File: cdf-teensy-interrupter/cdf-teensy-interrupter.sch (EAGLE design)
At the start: 20 parts

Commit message: wip
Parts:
- added EMERGENCY: SWITCH-MOMENTARY-2PTH, SparkFun-Electromechanical:SWITCH-MOMENTARY-2PTH
- added R7: 220, rcl:R-US_0204/7
- added SP1: SPEAKER/PS12, adafruit:SPEAKER/PS12
- added T1: BC337, transistor:BC337
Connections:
- new net EMERGENCY: EMERGENCY.1, U$2.11/MOSI
- new net N$11: SP1.+, T1.C, U$6.C
- new net N$7: R7.1, T1.B
- net +3V3: now also R3.2
- net +5V: now also R5.2, SP1.-; no longer R3.2
- net GND: now also EMERGENCY.2, T1.E; no longer U$6.C
- net TX: now also R7.2; no longer R5.2
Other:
- note added: "TL1105LF250Q"
- moved on the sheet: R5, U$6
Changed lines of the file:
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@@
 <part name="R2" library="rcl" deviceset="R-US_" device="0204/7" value="100K"/>
 <part name="R3" library="rcl" deviceset="R-US_" device="0204/7" value="3.3K"/>
-<part name="P+1" library="supply1" deviceset="+5V" device=""/>
 <part name="GND3" library="supply1" deviceset="GND" device=""/>
 <part name="GND8" library="supply1" deviceset="GND" device=""/>
@@
 <part name="GND10" library="supply1" deviceset="GND" device=""/>
 <part name="R5" library="rcl" deviceset="R-US_" device="0204/7" value="68"/>
-<part name="GND11" library="supply1" deviceset="GND" device=""/>
 <part name="R6" library="rcl" deviceset="R-US_" device="0204/7" value="330"/>
 <part name="LED1" library="adafruit" deviceset="LED" device="5MM"/>
@@
 <part name="PULSE_WIDTH" library="Bourns" deviceset="POTENTIOMETER" device="PTV09A_VERTICAL" value="10K PTV09A-4025F-B103"/>
 <part name="P+6" library="supply1" deviceset="+5V" device=""/>
+<part name="+3V6" library="supply1" deviceset="+3V3" device=""/>
+<part name="GND14" library="supply1" deviceset="GND" device=""/>
+<part name="EMERGENCY" library="SparkFun-Electromechanical" deviceset="SWITCH-MOMENTARY-2" device="PTH"/>
+<part name="SP1" library="adafruit" deviceset="SPEAKER" device="/PS12"/>
+<part name="T1" library="transistor" deviceset="BC337" device=""/>
+<part name="R7" library="rcl" deviceset="R-US_" device="0204/7" value="220"/>
+<part name="GND16" library="supply1" deviceset="GND" device=""/>
+<part name="P+1" library="supply1" deviceset="+5V" device=""/>
 </parts>
 <sheets>
 <sheet>
 <plain>
+<text x="17.78" y="63.5" size="1.778" layer="96" rot="R270">
+TL1105LF250Q
+</text>
 </plain>
 <instances>
@@
 <instance part="U$1" gate="G$1" x="-30.48" y="83.82"/>
 <instance part="MIDI_MODE" gate="G$1" x="127" y="66.04" smashed="yes" rot="R270"/>
-<instance part="U$6" gate="G$1" x="137.16" y="22.86" rot="R90"/>
+<instance part="U$6" gate="G$1" x="10.16" y="35.56"/>
 <instance part="R1" gate="G$1" x="-7.62" y="81.28"/>
 <instance part="D1" gate="G$1" x="0" y="78.74" rot="R90"/>
@@
 <instance part="R2" gate="G$1" x="22.86" y="91.44" rot="R90"/>
 <instance part="R3" gate="G$1" x="33.02" y="91.44" rot="R90"/>
-<instance part="P+1" gate="1" x="33.02" y="101.6"/>
 <instance part="GND3" gate="1" x="22.86" y="68.58"/>
 <instance part="GND8" gate="1" x="149.86" y="96.52" rot="R90"/>
 <instance part="GND9" gate="1" x="149.86" y="111.76" rot="R90"/>
 <instance part="GND10" gate="1" x="134.62" y="63.5" rot="R90"/>
-<instance part="R5" gate="G$1" x="127" y="22.86" rot="R180"/>
-<instance part="GND11" gate="1" x="147.32" y="22.86" rot="R90"/>
+<instance part="R5" gate="G$1" x="10.16" y="50.8" rot="R90"/>
 <instance part="R6" gate="G$1" x="-17.78" y="48.26" rot="R270"/>
 <instance part="LED1" gate="G$1" x="-17.78" y="38.1"/>
@@
 </instance>
 <instance part="P+6" gate="1" x="-17.78" y="58.42"/>
+<instance part="+3V6" gate="G$1" x="33.02" y="101.6"/>
+<instance part="GND14" gate="1" x="137.16" y="38.1" rot="R90"/>
+<instance part="EMERGENCY" gate="G$1" x="124.46" y="38.1" smashed="yes">
+<attribute name="NAME" x="121.92" y="40.64" size="1.778" layer="95"/>
+</instance>
+<instance part="SP1" gate="S1" x="0" y="33.02" rot="R90"/>
+<instance part="T1" gate="G$1" x="12.7" y="17.78" rot="MR0"/>
+<instance part="R7" gate="G$1" x="27.94" y="17.78"/>
+<instance part="GND16" gate="1" x="10.16" y="7.62"/>
+<instance part="P+1" gate="1" x="10.16" y="63.5"/>
 </instances>
 <busses>
@@
 </segment>
 <segment>
-<pinref part="U$6" gate="G$1" pin="C"/>
-<pinref part="GND11" gate="1" pin="GND"/>
-<wire x1="144.78" y1="22.86" x2="142.24" y2="22.86" width="0.1524" layer="91"/>
-</segment>
-<segment>
 <pinref part="LED1" gate="G$1" pin="C"/>
 <pinref part="GND12" gate="1" pin="GND"/>
@@
 <pinref part="GND13" gate="1" pin="GND"/>
 </segment>
+<segment>
+<pinref part="GND14" gate="1" pin="GND"/>
+<wire x1="134.62" y1="38.1" x2="129.54" y2="38.1" width="0.1524" layer="91"/>
+<pinref part="EMERGENCY" gate="G$1" pin="2"/>
+</segment>
+<segment>
+<pinref part="T1" gate="G$1" pin="E"/>
+<pinref part="GND16" gate="1" pin="GND"/>
+<wire x1="10.16" y1="10.16" x2="10.16" y2="12.7" width="0.1524" layer="91"/>
+</segment>
 </net>
 <net name="+5V" class="0">
-<segment>
-<pinref part="R3" gate="G$1" pin="2"/>
-<pinref part="P+1" gate="1" pin="+5V"/>
-<wire x1="33.02" y1="99.06" x2="33.02" y2="96.52" width="0.1524" layer="91"/>
-</segment>
 <segment>
 <pinref part="U$2" gate="G$1" pin="VIN"/>
@@
 <wire x1="-17.78" y1="53.34" x2="-17.78" y2="55.88" width="0.1524" layer="91"/>
 <pinref part="P+6" gate="1" pin="+5V"/>
+</segment>
+<segment>
+<pinref part="SP1" gate="S1" pin="-"/>
+<wire x1="0" y1="38.1" x2="0" y2="58.42" width="0.1524" layer="91"/>
+<wire x1="0" y1="58.42" x2="10.16" y2="58.42" width="0.1524" layer="91"/>
+<pinref part="R5" gate="G$1" pin="2"/>
+<wire x1="10.16" y1="58.42" x2="10.16" y2="55.88" width="0.1524" layer="91"/>
+<pinref part="P+1" gate="1" pin="+5V"/>
+<wire x1="10.16" y1="58.42" x2="10.16" y2="60.96" width="0.1524" layer="91"/>
+<junction x="10.16" y="58.42"/>
 </segment>
 </net>
@@
 <net name="TX" class="0">
 <segment>
-<pinref part="R5" gate="G$1" pin="2"/>
-<wire x1="121.92" y1="22.86" x2="116.84" y2="22.86" width="0.1524" layer="91"/>
-<label x="116.84" y="22.86" size="1.778" layer="95"/>
-</segment>
-<segment>
 <pinref part="U$2" gate="G$1" pin="21/A7/PWM"/>
 <wire x1="43.18" y1="17.78" x2="33.02" y2="17.78" width="0.1524" layer="91"/>
 <label x="33.02" y="17.78" size="1.778" layer="95"/>
+<pinref part="R7" gate="G$1" pin="2"/>
 </segment>
 </net>
@@
 <pinref part="R5" gate="G$1" pin="1"/>
 <pinref part="U$6" gate="G$1" pin="A"/>
-<wire x1="134.62" y1="22.86" x2="132.08" y2="22.86" width="0.1524" layer="91"/>
+<wire x1="10.16" y1="38.1" x2="10.16" y2="45.72" width="0.1524" layer="91"/>
 </segment>
 </net>
@@
 <pinref part="+3V5" gate="G$1" pin="+3V3"/>
 </segment>
+<segment>
+<pinref part="R3" gate="G$1" pin="2"/>
+<wire x1="33.02" y1="99.06" x2="33.02" y2="96.52" width="0.1524" layer="91"/>
+<pinref part="+3V6" gate="G$1" pin="+3V3"/>
+</segment>
 </net>
 <net name="LCD_EN" class="0">
@@
 <pinref part="R4" gate="G$1" pin="2"/>
 <wire x1="55.88" y1="93.98" x2="66.04" y2="93.98" width="0.1524" layer="91"/>
+</segment>
+</net>
+<net name="EMERGENCY" class="0">
+<segment>
+<pinref part="EMERGENCY" gate="G$1" pin="1"/>
+<wire x1="119.38" y1="38.1" x2="106.68" y2="38.1" width="0.1524" layer="91"/>
+<label x="99.06" y="38.1" size="1.778" layer="95"/>
+</segment>
+<segment>
+<pinref part="U$2" gate="G$1" pin="11/MOSI"/>
+<wire x1="43.18" y1="43.18" x2="33.02" y2="43.18" width="0.1524" layer="91"/>
+<label x="25.4" y="43.18" size="1.778" layer="95"/>
+</segment>
+</net>
+<net name="N$7" class="0">
+<segment>
+<pinref part="R7" gate="G$1" pin="1"/>
+<pinref part="T1" gate="G$1" pin="B"/>
+<wire x1="15.24" y1="17.78" x2="22.86" y2="17.78" width="0.1524" layer="91"/>
+</segment>
+</net>
+<net name="N$11" class="0">
+<segment>
+<pinref part="SP1" gate="S1" pin="+"/>
+<wire x1="0" y1="25.4" x2="0" y2="27.94" width="0.1524" layer="91"/>
+<pinref part="U$6" gate="G$1" pin="C"/>
+<wire x1="10.16" y1="22.86" x2="10.16" y2="25.4" width="0.1524" layer="91"/>
+<pinref part="T1" gate="G$1" pin="C"/>
+<wire x1="10.16" y1="25.4" x2="10.16" y2="30.48" width="0.1524" layer="91"/>
+<wire x1="0" y1="25.4" x2="10.16" y2="25.4" width="0.1524" layer="91"/>
+<junction x="10.16" y="25.4"/>
 </segment>
 </net>
@@
 </schematic>
 </drawing>
+<compatibility>
+<note version="6.3" minversion="6.2.2" severity="warning">
+Since Version 6.2.2 text objects can contain more than one line,
+which will not be processed correctly with this version.
+</note>
+</compatibility>
 </eagle>

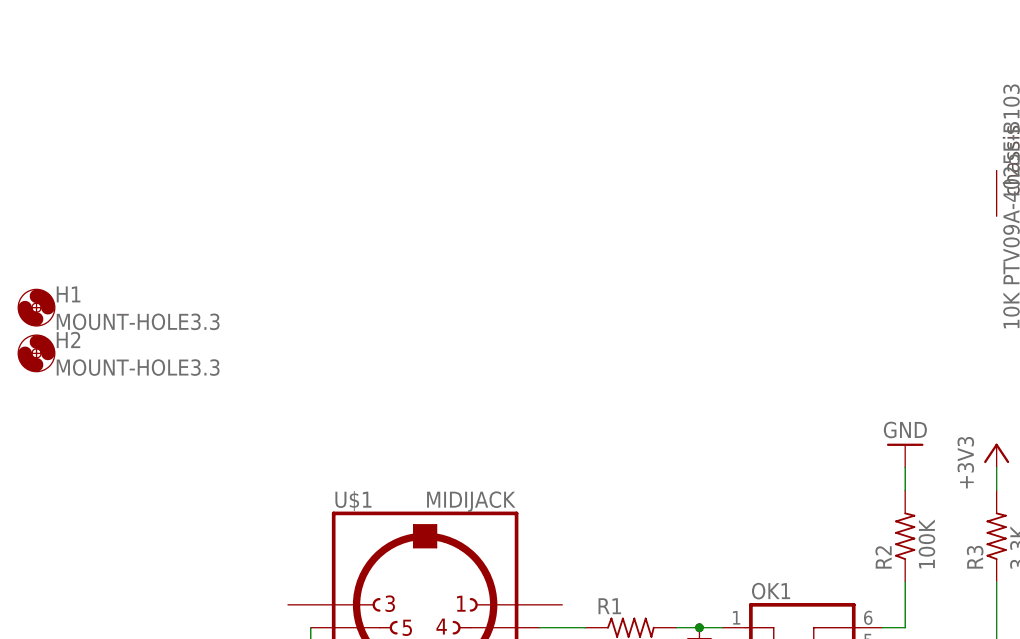
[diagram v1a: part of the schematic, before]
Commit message: add usb connector
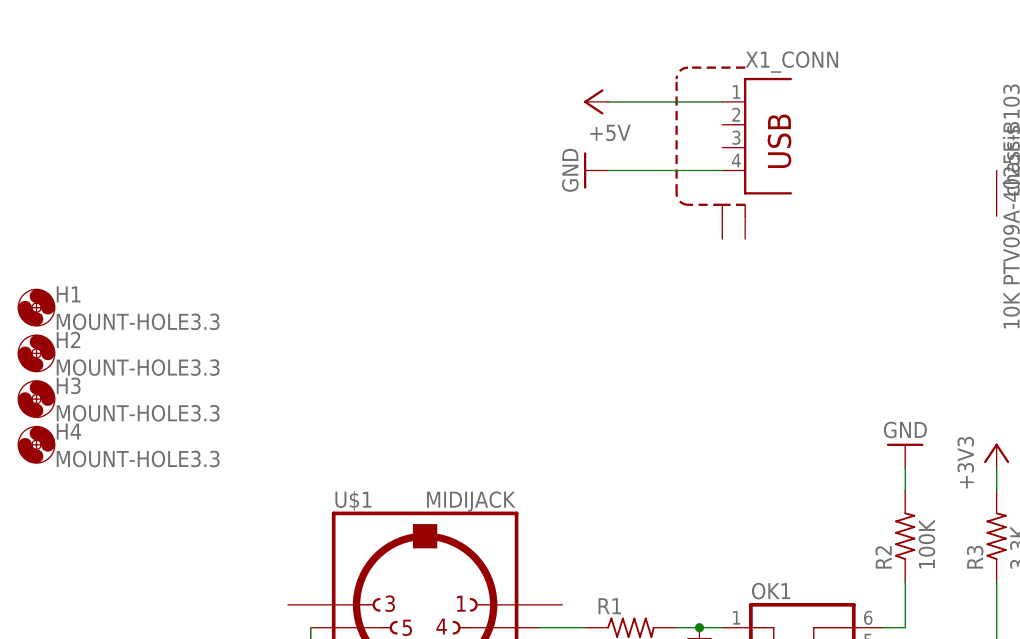
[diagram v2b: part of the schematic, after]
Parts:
- added H3, H4: MOUNT-HOLE3.3, holes:MOUNT-HOLE3.3
- added X1: (no value), keves:TE-292304-1
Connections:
- net +5V: now also X1_CONN.1
- net GND: now also X1_CONN.4
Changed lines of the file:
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@@
 <?xml version="1.0" encoding="utf-8"?>
 <!DOCTYPE eagle SYSTEM "eagle.dtd">
-<eagle version="7.5.0">
+<eagle version="7.3.0">
 <drawing>
 <settings>
@@
 <layers>
 <layer number="1" name="Top" color="4" fill="1" visible="no" active="no"/>
+<layer number="2" name="Route2" color="1" fill="3" visible="no" active="no"/>
+<layer number="3" name="Route3" color="4" fill="3" visible="no" active="no"/>
+<layer number="4" name="Route4" color="1" fill="4" visible="no" active="no"/>
+<layer number="5" name="Route5" color="4" fill="4" visible="no" active="no"/>
+<layer number="6" name="Route6" color="1" fill="8" visible="no" active="no"/>
+<layer number="7" name="Route7" color="4" fill="8" visible="no" active="no"/>
+<layer number="8" name="Route8" color="1" fill="2" visible="no" active="no"/>
+<layer number="9" name="Route9" color="4" fill="2" visible="no" active="no"/>
+<layer number="10" name="Route10" color="1" fill="7" visible="no" active="no"/>
+<layer number="11" name="Route11" color="4" fill="7" visible="no" active="no"/>
+<layer number="12" name="Route12" color="1" fill="5" visible="no" active="no"/>
+<layer number="13" name="Route13" color="4" fill="5" visible="no" active="no"/>
+<layer number="14" name="Route14" color="1" fill="6" visible="no" active="no"/>
+<layer number="15" name="Route15" color="4" fill="6" visible="no" active="no"/>
 <layer number="16" name="Bottom" color="1" fill="1" visible="no" active="no"/>
 <layer number="17" name="Pads" color="2" fill="1" visible="no" active="no"/>
@@
 <layer number="56" name="wert" color="7" fill="1" visible="no" active="no"/>
 <layer number="57" name="tCAD" color="7" fill="1" visible="no" active="no"/>
+<layer number="58" name="bCAD" color="11" fill="1" visible="no" active="no"/>
 <layer number="59" name="tCarbon" color="7" fill="1" visible="no" active="no"/>
 <layer number="60" name="bCarbon" color="7" fill="1" visible="no" active="no"/>
@@
 <part name="GND16" library="supply1" deviceset="GND" device=""/>
 <part name="P+1" library="supply1" deviceset="+5V" device=""/>
+<part name="X1" library="keves" deviceset="TE-292304-1" device=""/>
+<part name="GND11" library="supply1" deviceset="GND" device=""/>
+<part name="P+7" library="supply1" deviceset="+5V" device=""/>
+<part name="H3" library="holes" deviceset="MOUNT-HOLE" device="3.3"/>
+<part name="H4" library="holes" deviceset="MOUNT-HOLE" device="3.3"/>
 </parts>
 <sheets>
@@
 <instance part="GND16" gate="1" x="10.16" y="7.62"/>
 <instance part="P+1" gate="1" x="10.16" y="63.5"/>
+<instance part="X1" gate="_CONN" x="5.08" y="134.62"/>
+<instance part="X1" gate="SHIELD" x="2.54" y="137.16"/>
+<instance part="GND11" gate="1" x="-12.7" y="132.08" rot="R270"/>
+<instance part="P+7" gate="1" x="-12.7" y="139.7" rot="R90"/>
+<instance part="H3" gate="G$1" x="-73.66" y="106.68"/>
+<instance part="H4" gate="G$1" x="-73.66" y="101.6"/>
 </instances>
 <busses>
@@
 <wire x1="10.16" y1="10.16" x2="10.16" y2="12.7" width="0.1524" layer="91"/>
 </segment>
+<segment>
+<pinref part="X1" gate="_CONN" pin="4"/>
+<pinref part="GND11" gate="1" pin="GND"/>
+<wire x1="-10.16" y1="132.08" x2="2.54" y2="132.08" width="0.1524" layer="91"/>
+</segment>
 </net>
 <net name="+5V" class="0">
@@
 <junction x="10.16" y="58.42"/>
 </segment>
+<segment>
+<pinref part="X1" gate="_CONN" pin="1"/>
+<pinref part="P+7" gate="1" pin="+5V"/>
+<wire x1="-10.16" y1="139.7" x2="2.54" y2="139.7" width="0.1524" layer="91"/>
+</segment>
 </net>
